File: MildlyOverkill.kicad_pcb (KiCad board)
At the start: 4 copper layers, 195 x 124 mm, 186 parts, among them J1 USB_C_Receptacle_USB2.0_16P, J2 2604-1102, J3 2604-1104, J4 2604-1104, J5 Conn_01x04_Pin, J6 Conn_01x04_MountingPin, J7 Conn_01x02_Pin, J8 RJ45_Wuerth_7499010211A, M1 Fan_4pin, Q10 BTN8982TA, Q5 QM6015D, Q7 BTN8982TA, Q8 BTN8982TA, Q9 BTN8982TA, U1 ESP32-S3-WROOM-1, U2 MCP3208, U3 LD1117S33TR_SOT223, U4 TPS4H160AQPWPRQ1, U5 USBLC6-2P6, U6 TPS62932, U7 W5500, Y1 3134250001

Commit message: New refactor into a Smaler formfactor (2 Layer Possible?)
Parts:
- removed C17, C22, C23, C24, C25: 100nF, Capacitor_SMD:C_0603_1608Metric
- removed C19, C20: 1.5nF, Capacitor_SMD:C_0603_1608Metric
- removed D14, D15, D16, D17, D18, D19, D20, D21: SMAJ28A, Diode_SMD:D_SMA
- removed D9: 10V, Diode_SMD:D_SOD-123
- removed J7: Conn_01x02_Pin, Connector_PinHeader_2.54mm:PinHeader_1x02_P2.54mm_Vertical
- removed JP2, JP6, JP7, JP9: SolderJumper_3_Open, Jumper:SolderJumper-3_P2.0mm_Open_TrianglePad1.0x1.5mm_NumberLabels
- removed Q10, Q7, Q8, Q9: BTN8982TA, Package_TO_SOT_SMD:TO-263-7_TabPin8
- removed Q5: QM6015D, Package_TO_SOT_SMD:TO-252-2
- removed R20, R22, R24, R29, R31: 10k, Resistor_SMD:R_0805_2012Metric
- removed R21, R30: 500, Resistor_SMD:R_0805_2012Metric
- removed R23: 33k, Resistor_SMD:R_0805_2012Metric
- removed R25, R26, R27, R28: 3.3k, Resistor_SMD:R_0805_2012Metric
- removed R4: 10K, Resistor_SMD:R_0805_2012Metric
- removed R57, R58, R59, R60: 0R, Resistor_SMD:R_0805_2012Metric_Pad1.20x1.40mm_HandSolder
- removed R65, R69, R70, R72: R, Resistor_SMD:R_0805_2012Metric_Pad1.20x1.40mm_HandSolder
- removed R78, R79: R, Resistor_SMD:R_0805_2012Metric
- removed TH2: Thermistor_NTC, Connector_PinHeader_2.54mm:PinHeader_1x02_P2.54mm_Vertical
- removed TH3: Thermistor_NTC, Resistor_SMD:R_0805_2012Metric_Pad1.20x1.40mm_HandSolder
- added D1: LED, LED_SMD:LED_0603_1608Metric, F.Cu at (152.7, 107.5)
- added D2: LED, LED_SMD:LED_0603_1608Metric, F.Cu at (71.5, 67.6)
- added J9: Analog, TerminalBlock_Phoenix:TerminalBlock_Phoenix_MPT-0,5-4-2.54_1x04_P2.54mm_Horizontal, F.Cu at (125.0, 125.0)
- added U8: DRV8874PWPR, Snapeda:PWP0016J_L, F.Cu at (152.7, 113.0)
- added U9: DRV8874PWPR, Snapeda:PWP0016J_L, F.Cu at (69.1, 63.1)
- C15: value 1.5nF -> 0.1uF
- C18: value 1.5nF -> 0.022uF
- C6: value 1nF -> 0.022uF
- C7, C8, C9: value 1nF -> 0.1uF
- D11: value VSS -> LED
- D12: value 3.3V -> LED
- D13, D23: value 5V -> LED
- J2: value 2604-1102 -> Screw_Terminal_01x02; footprint wago1102:CONN2_2604-1102_WAG -> Connector_Phoenix_MSTB:PhoenixContact_MSTBA_2,5_2-G_1x02_P5.00mm_Horizontal
- J3: value 2604-1104 -> Motors; footprint wago1104:CONN4_2604-1104_WAG -> TerminalBlock_Phoenix:TerminalBlock_Phoenix_MPT-0,5-4-2.54_1x04_P2.54mm_Horizontal
- J4: value 2604-1104 -> IO; footprint wago1104:CONN4_2604-1104_WAG -> TerminalBlock_Phoenix:TerminalBlock_Phoenix_MPT-0,5-4-2.54_1x04_P2.54mm_Horizontal
- R10: value 10k -> 660
- R11: value 500 -> 3300
- R13: value 500 -> 1k
- R14: value 33k -> 10k
- R15, R17, R19: value 10k -> 1k
- R8: value 33k -> 3300
- R9: value 33k -> 660
- moved R18 255.6 mm to (24.6, 67.3), turned to 0 degrees
- moved R16 255.5 mm to (24.6, 61.5), turned to 0 degrees
- moved R12 255.3 mm to (20.2, 73.2), turned to 0 degrees
- moved R67 248.5 mm to (25.4, 45.1)
- moved J4 233.1 mm to (137.5, 125.0)
- moved JP4 230.7 mm to (54.2, 37.6), turned to 0 degrees
- moved R13 225.5 mm to (20.2, 76.2), turned to 0 degrees
- moved U2 222.7 mm to (22.2, 97.5), turned to 0 degrees
- moved R77 217.3 mm to (33.4, 70.3), turned to 0 degrees
- moved C18 215.6 mm to (63.1, 66.2), turned to 0 degrees
- moved TH1 210.3 mm to (25.4, 54.0), turned to 0 degrees
- moved R71 206.8 mm to (25.4, 51.0), turned to 0 degrees
- moved R64 203.9 mm to (25.4, 42.2), turned to 0 degrees
- moved R68 203.2 mm to (25.4, 48.1), turned to 0 degrees
- moved C9 187.7 mm to (63.1, 61.2)
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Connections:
- C15 pad 1: GPIO1 -> VCC
- C15 pad 2: GND -> Net-(U9-VCP)
- C18 pad 1: GPIO2 -> Net-(U9-CPH)
- C18 pad 2: GND -> Net-(U9-CPL)
- C6 pad 1: IS1 -> Net-(U8-CPH)
- C6 pad 2: GND -> Net-(U8-CPL)
- C7 pad 1: IS2 -> VCC
- C7 pad 2: GND -> Net-(U8-VCP)
- C8 pad 1: IS3 -> GND
- C8 pad 2: GND -> VCC
- C9 pad 1: IS4 -> GND
- C9 pad 2: GND -> VCC
- J2 pad 1: Net-(J2-1_1) -> GND
- J2 pad 2: Net-(J2-1_1) -> VCC
- J3 pad 1: IO3 -> M1.1
- J3 pad 2: IO3 -> M1.2
- J3 pad 3: IO1 -> M2.2
- J3 pad 4: IO1 -> M2.1
- J4 pad 1: IO7 -> IO1
- J4 pad 2: IO7 -> IO2
- J4 pad 3: IO5 -> IO3
- J4 pad 4: IO5 -> IO4
- R10 pad 1: Net-(Q7-IN) -> +3.3V
- R10 pad 2: GPIO1 -> Net-(D2-A)
- R11 pad 1: IS1 -> CURR1
- R12 pad 2: GPIO2 -> AIN1
- R13 pad 1: IS2 -> AIN1
- R14 pad 1: IO3 -> Net-(J9-Pin_2)
- R14 pad 2: GPIO3 -> AIN2
- R15 pad 1: EN1 -> AIN2
- R15 pad 2: Net-(Q7-INH) -> GND
- R16 pad 1: EN2 -> Net-(J9-Pin_3)
- R16 pad 2: Net-(Q8-INH) -> AIN3
- R17 pad 1: EN1 -> AIN3
- R18 pad 1: EN2 -> Net-(J9-Pin_4)
- R18 pad 2: GND -> AIN4
- R19 pad 1: Net-(Q9-IN) -> AIN4
- R19 pad 2: GPIO3 -> GND
- R33 pad 1: IO5 -> IO1
- R35 pad 1: IO6 -> IO2
- R37 pad 1: IO7 -> IO3
- R39 pad 1: IO8 -> IO4
- R8 pad 1: IO1 -> CURR2
- R8 pad 2: GPIO1 -> GND
- R9 pad 1: IO2 -> +3.3V
- R9 pad 2: GPIO2 -> Net-(D1-A)
- U1 pad 15: GPIO3 -> IN2.1
- U1 pad 19: EN1 -> unconnected-(U1-IO11-Pad19)
- U1 pad 20: EN2 -> unconnected-(U1-IO12-Pad20)
- U1 pad 21: EN3 -> unconnected-(U1-IO13-Pad21)
- U1 pad 22: EN4 -> unconnected-(U1-IO14-Pad22)
- U1 pad 24: Net-(J7-Pin_2) -> unconnected-(U1-IO47-Pad24)
- U1 pad 25: Net-(J7-Pin_1) -> unconnected-(U1-IO48-Pad25)
- U1 pad 38: GPIO2 -> IN1.2
- U1 pad 39: GPIO1 -> IN1.1
- U1 pad 4: GPIO4 -> IN2.2
- U2 pad 1: IS1 -> AIN1
- U2 pad 2: IS2 -> AIN2
- U2 pad 3: IS3 -> AIN3
- U2 pad 4: IS4 -> AIN4
- U2 pad 6: NTC2 -> CURR1
- U2 pad 7: NTC3 -> CURR2
- U4 pad 15: IO8 -> IO4
- U4 pad 16: IO8 -> IO4
- U4 pad 17: IO7 -> IO3
- U4 pad 18: IO7 -> IO3
- U4 pad 25: IO6 -> IO2
- U4 pad 26: IO6 -> IO2
- U4 pad 27: IO5 -> IO1
- U4 pad 28: IO5 -> IO1
- U7 pad 37: unconnected-(U7-~{RST}-Pad37) -> RST
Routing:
- net +3.3V: track 223.0 -> 0.00 mm, vias 137 -> 0
- net IS3: track 183.8 -> 0.00 mm, vias 2 -> 0
- net IS1: track 153.6 -> 0.00 mm, vias 2 -> 0
- net IS2: track 119.1 -> 0.00 mm, vias 2 -> 0
- net IS4: track 92.5 -> 0.00 mm, vias 2 -> 0
- net ETH_CS: track 65.7 -> 0.00 mm, vias 2 -> 0
- net ACT_LED: track 63.9 -> 0.00 mm, vias 2 -> 0
- net LINK_LED: track 57.4 -> 0.00 mm, vias 2 -> 0
- net MISO: track 54.7 -> 0.00 mm, vias 2 -> 0
- net SCLK: track 52.9 -> 0.00 mm, vias 2 -> 0
- net MOSI: track 51.8 -> 0.00 mm, vias 2 -> 0
- net GND: track 47.1 -> 0.00 mm, vias 307 -> 0
- net VCC: track 49.7 -> 4.28 mm, vias 202 -> 0
- net NTC1: track 41.2 -> 0.00 mm, vias 2 -> 0
- net RST: track 37.1 -> 0.00 mm, vias 2 -> 0
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- removed copper zone on B.Cu, net (none)
- removed copper zone on B.Cu, net +3.3V
- removed copper zone on F.Cu, net +3.3V
- removed copper zone on B.Cu, net +3.3VA
- removed copper zone on B.Cu, net +5V
- removed copper zone on F.Cu, net +5V
- removed copper zone on F.Cu, net /shield
- removed copper zone on F.Cu, net GND
- removed copper zone on In1.Cu, net GND
- removed copper zone on In2.Cu, net GND
- removed copper zone on B.Cu, net IO1
- removed copper zone on F.Cu, net IO1
- removed copper zone on B.Cu, net IO2
- removed copper zone on F.Cu, net IO2
- removed copper zone on B.Cu, net IO3
- removed copper zone on F.Cu, net IO3
- removed copper zone on B.Cu, net IO4
- removed copper zone on F.Cu, net IO4
- removed copper zone on B.Cu, net Net-(J2-1_1)
- removed copper zone on F.Cu, net Net-(J2-1_1)
- removed copper zone on B.Cu, net VCC
- removed copper zone on F.Cu, net VCC
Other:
- board size 195 x 124 mm -> 100 x 80 mm
- copper layers 4 -> 2
- board text removed: "BOOT"
- board text removed: "RST"

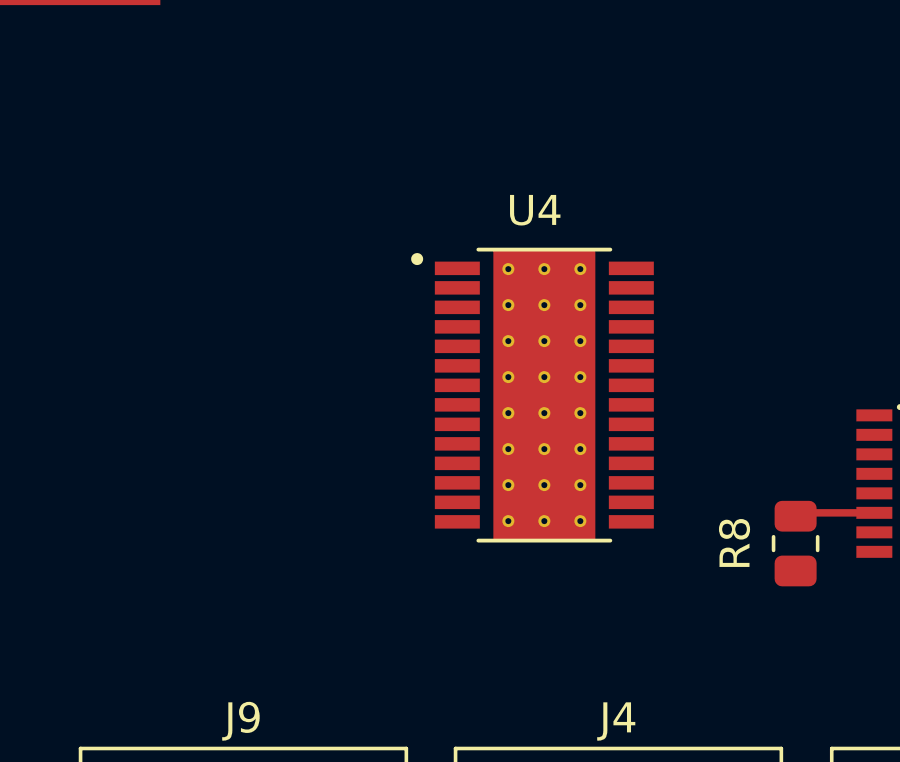
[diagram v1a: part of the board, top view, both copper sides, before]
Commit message: Added custom footprint and made Buck samller
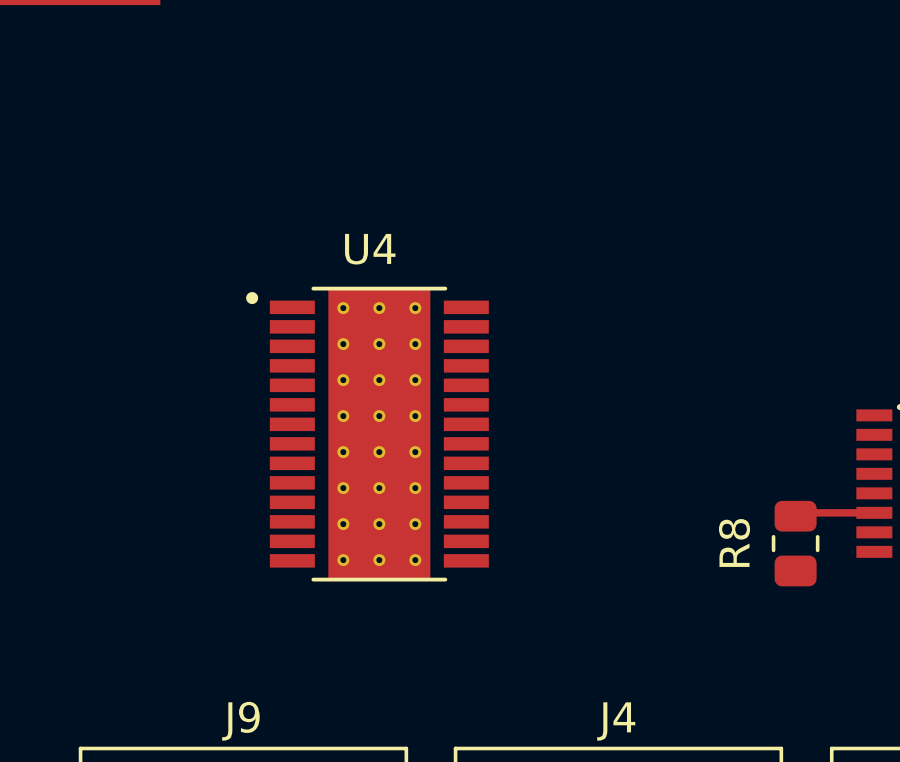
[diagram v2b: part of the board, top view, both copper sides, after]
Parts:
- moved U4 5.65 mm to (133.3, 111.3)
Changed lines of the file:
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@@
 	(footprint "TPS4H160AQPWPRQ1:IC_TPS4H160AQPWPRQ1"
 		(layer "F.Cu")
-		(at 138.8 110)
+		(at 133.3 111.3)
 		(property "Reference" "U4"
 			(at -0.325 -6.135 0)
@@
 	)
 	(segment
-		(start 156.377607 111.975002)
-		(end 157.4004 110.952209)
-		(width 0.25)
-		(layer "F.Cu")
-		(net "Net-(U8-CPL)")
-	)
-	(segment
-		(start 157.4004 110.952209)
-		(end 157.4004 109.450001)
-		(width 0.25)
-		(layer "F.Cu")
-		(net "Net-(U8-CPL)")
-	)
-	(segment
-		(start 155.499999 111.975002)
-		(end 156.377607 111.975002)
-		(width 0.25)
-		(layer "F.Cu")
-		(net "Net-(U8-CPL)")
-	)
-	(segment
-		(start 158.6754 110.950001)
-		(end 158.9504 110.675001)
-		(width 0.25)
-		(layer "F.Cu")
-		(net "Net-(U8-CPH)")
-	)
-	(segment
-		(start 158.039004 110.950001)
-		(end 158.6754 110.950001)
-		(width 0.25)
-		(layer "F.Cu")
-		(net "Net-(U8-CPH)")
-	)
-	(segment
-		(start 155.499999 112.625003)
-		(end 156.364002 112.625003)
-		(width 0.25)
-		(layer "F.Cu")
-		(net "Net-(U8-CPH)")
-	)
-	(segment
-		(start 158.9504 110.675001)
-		(end 158.9504 109.450001)
-		(width 0.25)
-		(layer "F.Cu")
-		(net "Net-(U8-CPH)")
-	)
-	(segment
-		(start 156.364002 112.625003)
-		(end 158.039004 110.950001)
-		(width 0.25)
-		(layer "F.Cu")
-		(net "Net-(U8-CPH)")
-	)
-	(segment
 		(start 158.2254 113.675001)
 		(end 158.1754 113.725001)
@@
 		(net "CURR2")
 	)
+	(segment
+		(start 158.6754 110.950001)
+		(end 158.9504 110.675001)
+		(width 0.25)
+		(layer "F.Cu")
+		(net "Net-(U8-CPH)")
+	)
+	(segment
+		(start 158.039004 110.950001)
+		(end 158.6754 110.950001)
+		(width 0.25)
+		(layer "F.Cu")
+		(net "Net-(U8-CPH)")
+	)
+	(segment
+		(start 155.499999 112.625003)
+		(end 156.364002 112.625003)
+		(width 0.25)
+		(layer "F.Cu")
+		(net "Net-(U8-CPH)")
+	)
+	(segment
+		(start 158.9504 110.675001)
+		(end 158.9504 109.450001)
+		(width 0.25)
+		(layer "F.Cu")
+		(net "Net-(U8-CPH)")
+	)
+	(segment
+		(start 156.364002 112.625003)
+		(end 158.039004 110.950001)
+		(width 0.25)
+		(layer "F.Cu")
+		(net "Net-(U8-CPH)")
+	)
+	(segment
+		(start 156.377607 111.975002)
+		(end 157.4004 110.952209)
+		(width 0.25)
+		(layer "F.Cu")
+		(net "Net-(U8-CPL)")
+	)
+	(segment
+		(start 157.4004 110.952209)
+		(end 157.4004 109.450001)
+		(width 0.25)
+		(layer "F.Cu")
+		(net "Net-(U8-CPL)")
+	)
+	(segment
+		(start 155.499999 111.975002)
+		(end 156.377607 111.975002)
+		(width 0.25)
+		(layer "F.Cu")
+		(net "Net-(U8-CPL)")
+	)
 	(embedded_fonts no)

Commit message: H-Bridges are done i guess
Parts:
- added R57: 10.7K, Resistor_SMD:R_0805_2012Metric, F.Cu at (74.2, 87.5)
- C10: value 24pF -> 5.6pF
- L1: value 12uH -> 3.3uH; footprint Inductor_SMD:L_Bourns_SRR1208_12.7x12.7mm -> Library:WE-XHMI 4.3x4.3
- moved C9 93.7 mm to (147.6, 101.7)
- moved C15 93.2 mm to (147.6, 103.1), turned to 180 degrees
- moved R11 92.2 mm to (148.9, 113.8)
- moved U9 90.6 mm to (147.5, 108.7), turned to 90 degrees
- moved C18 88.9 mm to (144.0, 103.1), turned to -90 degrees
- moved R10 85.9 mm to (143.5, 107.3), turned to -90 degrees
- moved D2 83.9 mm to (143.5, 110.8), turned to 90 degrees
- moved R8 16.5 mm to (156.5, 101.3), turned to 180 degrees
- moved J4 12.5 mm to (124.9, 125.0)
- moved J9 12.5 mm to (137.4, 125.0)
- moved D1 9.68 mm to (161.9, 104.3), turned to -90 degrees
- moved R9 9.48 mm to (161.9, 107.8), turned to 90 degrees
- moved U8 8.32 mm to (157.9, 106.5), turned to -90 degrees
- moved C16 7.52 mm to (174.5, 95.0)
- moved U4 4.93 mm to (128.6, 112.8), turned to -90 degrees
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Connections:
- U4 pad 15: IO4 -> IO1
- U4 pad 16: IO4 -> IO1
- U4 pad 17: IO3 -> IO2
- U4 pad 18: IO3 -> IO2
- U4 pad 25: IO2 -> IO3
- U4 pad 26: IO2 -> IO3
- U4 pad 27: IO1 -> IO4
- U4 pad 28: IO1 -> IO4
- U4 pad 3: OUT5 -> OUT8
- U4 pad 4: OUT6 -> OUT7
- U4 pad 5: OUT7 -> OUT6
- U4 pad 6: OUT8 -> OUT5
- U6 pad 1: unconnected-(U6-RT-Pad1) -> Net-(U6-RT)
- U8 pad 1: IN2.2 -> IN2.1
- U8 pad 10: M2.2 -> M2.1
- U8 pad 2: IN2.1 -> IN2.2
- U8 pad 8: M2.1 -> M2.2
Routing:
- net VCC: track 4.28 -> 108.2 mm, vias 0 -> 6
- net M1.2: track 0.00 -> 24.8 mm
- net M2.2: track 0.00 -> 22.5 mm
- net M2.1: track 0.00 -> 16.8 mm
- net M1.1: track 0.00 -> 15.3 mm
- net +3.3V: track 0.00 -> 8.39 mm, vias 0 -> 4
- net Net-(D2-K): track 0.00 -> 6.89 mm
- net Net-(D1-K): track 0.00 -> 6.89 mm
- net Net-(U9-CPH): track 0.00 -> 5.48 mm
- net Net-(U9-CPL): track 0.00 -> 3.83 mm
- net Net-(U9-VCP): track 0.00 -> 3.42 mm
- net CURR1: track 0.00 -> 2.50 mm
- net (no net): track 2.00 -> 0.00 mm
- net Net-(D2-A): track 0.00 -> 1.80 mm
- net Net-(D1-A): track 0.00 -> 1.80 mm
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- added copper zone on In1.Cu, net GND
- added copper zone on F.Cu, net IO1
- added copper zone on F.Cu, net IO2
- added copper zone on F.Cu, net IO3
- added copper zone on F.Cu, net IO4
- added copper zone on B.Cu, net VCC
- added copper zone on F.Cu, net VCC
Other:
- copper layers 2 -> 4

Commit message: Power stage almost done
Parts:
- added C17: 10uF, Capacitor_SMD:C_0603_1608Metric, F.Cu at (148.5, 69.2)
- added D3: BZT52C15, Diode_SMD:D_0805_2012Metric, F.Cu at (173.0, 73.5)
- added D4: SMAJ33A, Diode_SMD:D_SMA, F.Cu at (158.0, 68.0)
- added F1: Fuse, Fuse:Fuseholder_Blade_Mini_Keystone_3568, F.Cu at (166.2, 57.5)
- added Q1: Q_PMOS_GDS, Package_TO_SOT_SMD:TO-252-2, F.Cu at (165.5, 75.3)
- added R4: 100, Resistor_SMD:R_0805_2012Metric, F.Cu at (173.0, 77.1)
- moved U7 170.8 mm to (1.85, 109.7)
- moved D22 145.6 mm to (144.9, 69.6), turned to -90 degrees
- moved R18 141.3 mm to (156.5, 118.0), turned to 90 degrees
- moved R17 138.7 mm to (152.5, 118.0), turned to -90 degrees
- moved R19 138.4 mm to (154.5, 118.0), turned to -90 degrees
- moved R16 138.0 mm to (150.5, 118.0), turned to 90 degrees
- moved U6 134.6 mm to (147.6, 79.3), turned to 180 degrees
- moved R14 134.1 mm to (148.5, 118.0), turned to 90 degrees
- moved R12 132.1 mm to (144.5, 118.0), turned to 90 degrees
- moved R15 131.4 mm to (146.6, 118.0), turned to -90 degrees
- moved C14 131.2 mm to (155.4, 78.6), turned to -90 degrees
- moved R13 129.3 mm to (142.5, 118.0), turned to -90 degrees
- moved U2 126.2 mm to (148.0, 106.6)
- moved C13 120.0 mm to (152.4, 78.6), turned to -90 degrees
- moved C10 117.7 mm to (146.7, 84.2), turned to -90 degrees
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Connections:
- C10 pad 2: Net-(D22-A) -> +5V
- J2 pad 2: VCC -> Net-(J2-Pin_2)
- R55 pad 1: Net-(D22-A) -> +5V
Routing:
- net VCC: track 108.2 -> 151.2 mm, vias 6 -> 5
- net +3.3V: track 8.39 -> 45.2 mm, vias 4 -> 8
- net CURR2: track 2.50 -> 39.0 mm, vias 0 -> 2
- net +5V: track 0.00 -> 33.4 mm, vias 0 -> 2
- net CURR1: track 2.50 -> 28.2 mm, vias 0 -> 2
- net AIN4: track 0.00 -> 24.9 mm
- net AIN3: track 0.00 -> 23.0 mm
- net ST: track 0.00 -> 22.1 mm, vias 0 -> 2
- net AIN2: track 0.00 -> 21.1 mm
- net AIN1: track 0.00 -> 19.5 mm
- net GND: track 0.00 -> 14.2 mm, vias 0 -> 19
- net Net-(U6-FB): track 0.00 -> 8.53 mm
- net Net-(J9-Pin_4): track 0.00 -> 7.07 mm
- net Net-(J9-Pin_1): track 0.00 -> 6.65 mm
- net Net-(J9-Pin_3): track 0.00 -> 6.27 mm
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- added copper zone on In2.Cu, net +3.3V
- added copper zone on B.Cu, net GND
- added copper zone on F.Cu, net GND
- added copper zone on F.Cu, net Net-(D22-A)
- added copper zone on B.Cu, net Net-(D4-A1)
- added copper zone on F.Cu, net Net-(D4-A1)
- added copper zone on B.Cu, net Net-(J2-Pin_2)
- added copper zone on F.Cu, net Net-(J2-Pin_2)
- added copper zone on F.Cu, net Net-(U6-SW)

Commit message: Insane amounts of routing and Ethernet ist basicaly done.
DRC is going to be fun for future me...
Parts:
- removed D11, D12, D13, D23: LED, LED_SMD:LED_0603_1608Metric
- removed JP1, JP4, JP5, JP8: SolderJumper_3_Open, Jumper:SolderJumper-3_P2.0mm_Open_TrianglePad1.0x1.5mm_NumberLabels
- removed R52: 10k, Resistor_SMD:R_0805_2012Metric
- removed R53, R61: 210, Resistor_SMD:R_0805_2012Metric
- removed R54: 400, Resistor_SMD:R_0805_2012Metric
- removed R71: R, Resistor_SMD:R_0805_2012Metric_Pad1.20x1.40mm_HandSolder
- removed TP1: GND, TestPoint:TestPoint_Loop_D2.50mm_Drill1.85mm
- removed TP2: VCC, TestPoint:TestPoint_Loop_D2.50mm_Drill1.85mm
- removed TP3: 3.3V, TestPoint:TestPoint_Loop_D2.50mm_Drill1.85mm
- removed TP4: 5V, TestPoint:TestPoint_Loop_D2.50mm_Drill1.85mm
- added R65: 33, Resistor_SMD:R_0603_1608Metric, F.Cu at (110.8, 99.5)
- added kibuzzard-6AB94CCA: G***, kibuzzard-6AB94CCA, F.Cu at (149.9, 119.4)
- added kibuzzard-6AB94CD2: G***, kibuzzard-6AB94CD2, F.Cu at (152.4, 119.4)
- added kibuzzard-6AB94CD7: G***, kibuzzard-6AB94CD7, F.Cu at (154.9, 119.4)
- added kibuzzard-6AB94CDC: G***, kibuzzard-6AB94CDC, F.Cu at (147.3, 119.4)
- added kibuzzard-6AB94D65: G***, kibuzzard-6AB94D65, F.Cu at (130.8, 119.4)
- added kibuzzard-6AB94D6B: G***, kibuzzard-6AB94D6B, F.Cu at (133.3, 119.4)
- added kibuzzard-6AB94D6F: G***, kibuzzard-6AB94D6F, F.Cu at (135.9, 119.4)
- added kibuzzard-6AB94D73: G***, kibuzzard-6AB94D73, F.Cu at (138.4, 119.4)
- C29, C30, C31, C32: footprint Capacitor_SMD:C_0805_2012Metric -> Capacitor_SMD:C_0603_1608Metric
- R42, R43, R44, R62, R66: footprint Resistor_SMD:R_0805_2012Metric -> Resistor_SMD:R_0603_1608Metric
- R64, R67, R68: value R -> 33; footprint Resistor_SMD:R_0805_2012Metric_Pad1.20x1.40mm_HandSolder -> Resistor_SMD:R_0603_1608Metric
- R74: footprint Capacitor_SMD:C_0603_1608Metric_Pad1.08x0.95mm_HandSolder -> Resistor_SMD:R_0805_2012Metric_Pad1.20x1.40mm_HandSolder
- Y1: footprint Crystal:Crystal_SMD_3225-4Pin_3.2x2.5mm_HandSoldering -> Crystal:Crystal_SMD_3225-4Pin_3.2x2.5mm
- moved C4 171.1 mm to (128.5, 70.0), turned to -90 degrees
- moved TH1 165.3 mm to (158.5, 95.5)
- moved C27 164.2 mm to (123.3, 79.4), turned to 90 degrees
- moved FB2 154.5 mm to (125.0, 88.0), turned to -90 degrees
- moved C2 151.4 mm to (152.5, 102.0), turned to -90 degrees
- moved R1 149.9 mm to (131.0, 52.5), turned to -90 degrees
- moved Y1 147.2 mm to (117.0, 77.2)
- moved R77 139.3 mm to (140.5, 102.0)
- moved C3 139.2 mm to (143.0, 65.2)
- moved C42 138.1 mm to (105.0, 115.5), turned to 90 degrees
- moved R74 138.1 mm to (114.8, 80.2)
- moved C35 136.7 mm to (125.5, 92.0)
- moved D5 136.0 mm to (97.2, 76.5), turned to 90 degrees
- moved FB1 133.9 mm to (97.2, 72.0), turned to -90 degrees
- moved R41 131.9 mm to (123.5, 95.0)
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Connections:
- net Net-(J8-RD+) renamed /ETH_RX_C_P
- net Net-(J8-RD-) renamed /ETH_RX_C_N
- C30 pad 1: Net-(U7-RXN) -> /ETH_RX_B_N
- C31 pad 1: Net-(U7-RXP) -> /ETH_RX_B_P
- J8 pad 1: Net-(J8-TD+) -> /ETH_TX_B_P
- J8 pad 2: Net-(J8-TD-) -> /ETH_TX_B_N
- R42 pad 1: Net-(U7-RXP) -> /ETH_RX_B_P
- R43 pad 1: Net-(U7-RXN) -> /ETH_RX_B_N
- R44 pad 2: Net-(J8-TD+) -> /ETH_TX_B_P
- R62 pad 2: Net-(J8-TD-) -> /ETH_TX_B_N
- R64 pad 1: IO1 -> /ETH_TX_A_N
- R64 pad 2: Net-(JP1-C) -> /ETH_TX_B_N
- R67 pad 1: IO2 -> /ETH_RX_A_N
- R67 pad 2: Net-(JP4-C) -> /ETH_RX_B_N
- R68 pad 1: IO3 -> /ETH_RX_A_P
- R68 pad 2: Net-(JP5-C) -> /ETH_RX_B_P
- U7 pad 1: Net-(J8-TD-) -> /ETH_TX_A_N
- U7 pad 2: Net-(J8-TD+) -> /ETH_TX_A_P
- U7 pad 5: Net-(U7-RXN) -> /ETH_RX_A_N
- U7 pad 6: Net-(U7-RXP) -> /ETH_RX_A_P
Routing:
- net MISO: track 0.00 -> 110.9 mm, vias 0 -> 4
- net MOSI: track 0.00 -> 110.8 mm, vias 0 -> 4
- net SCLK: track 0.00 -> 103.3 mm, vias 0 -> 4
- net CS_ADC: track 0.00 -> 89.8 mm, vias 0 -> 2
- net RST: track 0.00 -> 81.5 mm, vias 0 -> 3
- net +5V: track 33.4 -> 87.7 mm, vias 2 -> 3
- net ACT_LED: track 0.00 -> 53.7 mm, vias 0 -> 2
- net +3.3V: track 45.2 -> 98.5 mm, vias 8 -> 158
- net LINK_LED: track 0.00 -> 46.6 mm, vias 0 -> 2
- net NTC1: track 2.15 -> 34.6 mm, vias 1 -> 4
- net +3.3VA: track 0.00 -> 32.3 mm, vias 0 -> 6
- net ETH_CS: track 0.00 -> 31.5 mm, vias 0 -> 2
- net GND: track 14.2 -> 45.2 mm, vias 19 -> 87
- net Net-(U1-IO0): track 0.00 -> 25.8 mm
- net /shield: track 0.00 -> 24.6 mm
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- added copper zone on F.Cu, net +3.3V
- added copper zone on In2.Cu, net +3.3VA
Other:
- board text added: "Track width: (etehrnet) 0.5 oz inner:0.3051 1oz inner: 0,2722mm spacing: 0.5mm"
